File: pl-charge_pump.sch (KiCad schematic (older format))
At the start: 55 parts

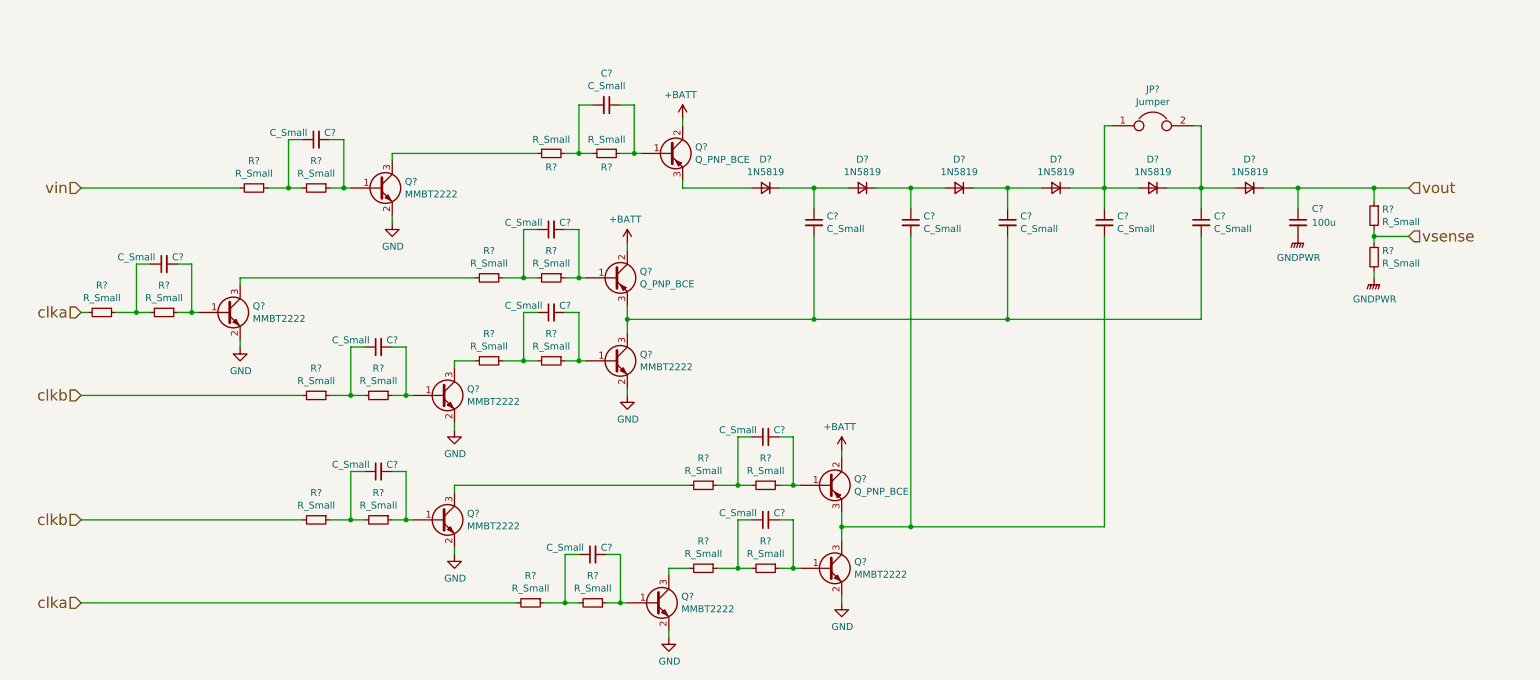
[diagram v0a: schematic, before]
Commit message: Added component values
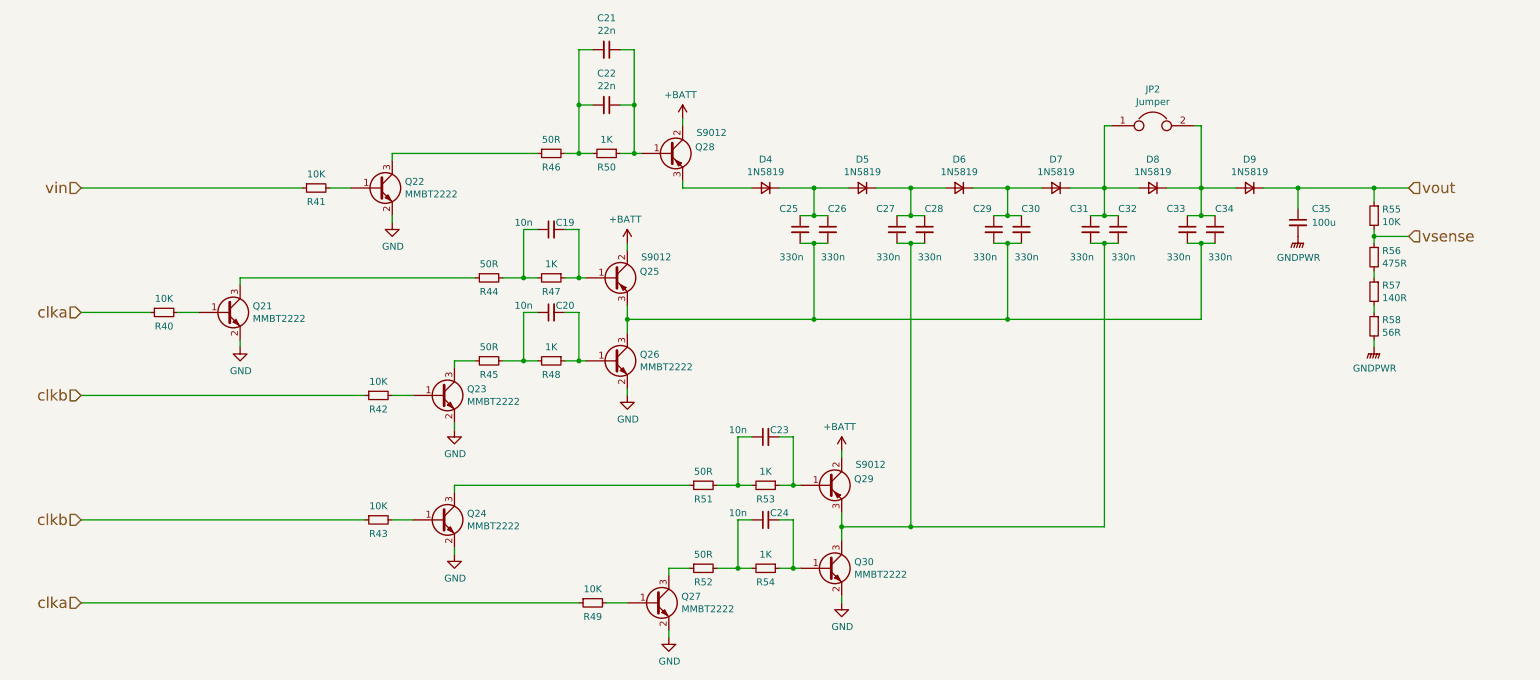
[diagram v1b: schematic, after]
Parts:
- removed C? (x13): C_Small, symbol Device:C_Small
- removed Q? (x2): Q_PNP_BCE, symbol Device:Q_PNP_BCE
- removed R? (x18): R_Small, symbol Device:R_Small
- added C20, C23, C24: 10n, symbol Device:C_Small
- added C21: 22n, symbol Device:C_Small
- added C25, C26, C27, C28, C29, C30, C31, C32, C33, C34: 330n, symbol Device:C_Small
- added Q25, Q29: S9012, symbol Device:Q_PNP_BCE
- added R40, R41, R42, R43, R49: 10K, symbol Device:R_Small
- added R44, R45, R51, R52: 50R, symbol Device:R_Small
- added R47, R48, R53, R54: 1K, symbol Device:R_Small
- added R56: 475R, symbol Device:R_Small
- added R57: 140R, symbol Device:R_Small
- C19: renamed from C?; value C_Small -> 10n
- C22: renamed from C?; value C_Small -> 22n
- Q28: renamed from Q?; value Q_PNP_BCE -> S9012
- R46: renamed from R?; value R_Small -> 50R
- R50: renamed from R?; value R_Small -> 1K
- R55: renamed from R?; value R_Small -> 10K
- R58: renamed from R?; value R_Small -> 56R
- gave numbers to parts that had none: 15
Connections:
- net +BATT: now also Q25.2 (C), Q29.2 (C)
- net clka: now also R40.1, R49.1
- net clkb: now also R42.1, R43.1
- net vin: now also R41.1
- net vsense: now also R56.1; no longer R58.1
- net at C22.1, Q28.1 (B), R50.1: now also C21.1
- net at C22.2, R46.2, R50.2: now also C21.2
- net at D4.1 (K), D5.2 (A): now also C25.1, C26.1
- net at Q26.3 (C): now also C25.2, C26.2, C29.2, C30.2, C33.2, C34.2, Q25.3 (E)
- net at Q26.1 (B): now also C20.2, R48.1
- net at D5.1 (K), D6.2 (A): now also C27.1, C28.1
- net at Q30.3 (C): now also C27.2, C28.2, C31.2, C32.2, Q29.3 (E)
- net at D6.1 (K), D7.2 (A): now also C29.1, C30.1
- net at D7.1 (K), D8.2 (A), JP2.1: now also C31.1, C32.1
- net at D8.1 (K), D9.2 (A), JP2.2: now also C33.1, C34.1
- net at C19.2: now also Q25.1 (B), R47.1
- net at C19.1: now also R44.2, R47.2
- net at Q21.3 (C): now also R44.1
- net at Q23.3 (C): now also R45.1
- net at Q21.1 (B): now also R40.2
- net at Q23.1 (B): now also R42.2
- net at Q30.1 (B): now also C24.2, R54.1
- net at Q24.3 (C): now also R51.1
- net at Q27.3 (C): now also R52.1
- net at Q24.1 (B): now also R43.2
- net at Q27.1 (B): now also R49.2
- net at Q22.1 (B): now also R41.2
- new net: R56.2, R57.1
- new net: R57.2, R58.1
- new net: C20.1, R45.2, R48.2
- new net: C23.1, R51.2, R53.2
- new net: C23.2, Q29.1 (B), R53.1
- new net: C24.1, R52.2, R54.2
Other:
- moved on the sheet: R58

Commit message: Schematics redesigned and fixed
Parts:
- removed C21: 22n, symbol Device:C_Small
- removed JP2: Jumper, symbol Device:Jumper
- removed R44, R45, R52: 50R, symbol Device:R_Small
- added R50, R57, R58: 56R, Capacitor_SMD:C_0805_2012Metric_Pad1.15x1.40mm_HandSolder, symbol Device:R_Small
- C21: renamed from C20; footprint (none) -> Capacitor_SMD:C_0805_2012Metric_Pad1.15x1.40mm_HandSolder
- C22: value 22n -> 10n-big; footprint (none) -> Capacitor_SMD:C_1206_3216Metric_Pad1.42x1.75mm_HandSolder
- C23: renamed from C19; footprint (none) -> Capacitor_SMD:C_0805_2012Metric_Pad1.15x1.40mm_HandSolder
- C24: renamed from C23; footprint (none) -> Capacitor_SMD:C_0805_2012Metric_Pad1.15x1.40mm_HandSolder
- C25: renamed from C24; footprint (none) -> Capacitor_SMD:C_0805_2012Metric_Pad1.15x1.40mm_HandSolder
- C26: renamed from C25; footprint (none) -> Capacitor_SMD:C_1206_3216Metric_Pad1.42x1.75mm_HandSolder
- C27: renamed from C26; footprint (none) -> Capacitor_SMD:C_1206_3216Metric_Pad1.42x1.75mm_HandSolder
- C28: renamed from C27; footprint (none) -> Capacitor_SMD:C_1206_3216Metric_Pad1.42x1.75mm_HandSolder
- C29: renamed from C28; footprint (none) -> Capacitor_SMD:C_1206_3216Metric_Pad1.42x1.75mm_HandSolder
- C30: renamed from C29; footprint (none) -> Capacitor_SMD:C_1206_3216Metric_Pad1.42x1.75mm_HandSolder
- C31: renamed from C30; footprint (none) -> Capacitor_SMD:C_1206_3216Metric_Pad1.42x1.75mm_HandSolder
- C32: renamed from C31; footprint (none) -> Capacitor_SMD:C_1206_3216Metric_Pad1.42x1.75mm_HandSolder
- C33: renamed from C32; footprint (none) -> Capacitor_SMD:C_1206_3216Metric_Pad1.42x1.75mm_HandSolder
- C34: renamed from C33; footprint (none) -> Capacitor_SMD:C_1206_3216Metric_Pad1.42x1.75mm_HandSolder
- C35: renamed from C34; footprint (none) -> Capacitor_SMD:C_1206_3216Metric_Pad1.42x1.75mm_HandSolder
- C36: renamed from C35; footprint (none) -> Capacitor_SMD:CP_Elec_6.3x5.9
- D4, D5, D6, D7, D8, D9: footprint (none) -> Diode_SMD:D_SMA_Handsoldering
- Q25, Q28, Q29: footprint (none) -> Package_TO_SOT_SMD:SOT-23
- R46: renamed from R40; footprint (none) -> Capacitor_SMD:C_0805_2012Metric_Pad1.15x1.40mm_HandSolder
- R47: renamed from R41; footprint (none) -> Capacitor_SMD:C_0805_2012Metric_Pad1.15x1.40mm_HandSolder
- R48: renamed from R42; footprint (none) -> Capacitor_SMD:C_0805_2012Metric_Pad1.15x1.40mm_HandSolder
- R49: renamed from R43; footprint (none) -> Capacitor_SMD:C_0805_2012Metric_Pad1.15x1.40mm_HandSolder
- R51: value 50R -> 56R; footprint (none) -> Capacitor_SMD:C_0805_2012Metric_Pad1.15x1.40mm_HandSolder
- R52: renamed from R46; value 50R -> 56R; footprint (none) -> Capacitor_SMD:C_0805_2012Metric_Pad1.15x1.40mm_HandSolder
- R53: renamed from R47; footprint (none) -> Resistor_SMD:R_0603_1608Metric_Pad1.05x0.95mm_HandSolder
- R54: renamed from R48; footprint (none) -> Resistor_SMD:R_0603_1608Metric_Pad1.05x0.95mm_HandSolder
- R55: renamed from R49; footprint (none) -> Capacitor_SMD:C_0805_2012Metric_Pad1.15x1.40mm_HandSolder
- R56: renamed from R50; footprint (none) -> Resistor_SMD:R_0603_1608Metric_Pad1.05x0.95mm_HandSolder
- R59: renamed from R53; footprint (none) -> Resistor_SMD:R_0603_1608Metric_Pad1.05x0.95mm_HandSolder
- R60: renamed from R54; footprint (none) -> Resistor_SMD:R_0603_1608Metric_Pad1.05x0.95mm_HandSolder
- R61: renamed from R55; footprint (none) -> Capacitor_SMD:C_0805_2012Metric_Pad1.15x1.40mm_HandSolder
- R62: renamed from R56; footprint (none) -> Capacitor_SMD:C_1206_3216Metric_Pad1.42x1.75mm_HandSolder
- R63: renamed from R57; footprint (none) -> Capacitor_SMD:C_1206_3216Metric_Pad1.42x1.75mm_HandSolder
- R64: renamed from R58; footprint (none) -> Capacitor_SMD:C_0805_2012Metric_Pad1.15x1.40mm_HandSolder
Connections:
- net GND is gone; now on net GNDPWR: Q21.2 (E), Q22.2 (E), Q23.2 (E), Q24.2 (E), Q26.2 (E), Q27.2 (E), Q30.2 (E)
- net GNDPWR: no longer R64.2
- net at Q28.1 (B), R56.1: now also C23.2; no longer C22.1
- net at R52.2, R56.2: now also C23.1; no longer C22.2
- net at Q26.1 (B), R54.1: now also C22.1; no longer C21.2
- net at R53.2: now also C21.1, R50.2; no longer C23.1
- net at Q25.1 (B), R53.1: now also C21.2; no longer C23.2
- net at R54.2: now also C22.2, R51.2; no longer C21.1
- net at C24.1, R59.2: now also R57.2; no longer R51.2
- net at C25.1, R60.2: now also R58.2
- net at Q21.3 (C): now also R50.1
- net at Q23.3 (C): now also R51.1
- net at Q24.3 (C): now also R57.1; no longer R51.1
- net at Q27.3 (C): now also R58.1
- net +BATT renamed +BATT-1
- net vin renamed onoff
- new net vsense_gnd: R64.2
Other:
- moved on the sheet: C21, C22, C23
